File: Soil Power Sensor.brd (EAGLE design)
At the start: 94 x 67 mm, 92 parts, among them IC1 TPD2E2U06DCK, J1 12401832E402A, U1 MAX9943ATT+, U10 FT234XD, U11 ESP32-C3-MINI-1-N4, U2 INA296A5, U3 THS4532, U4 FSA2466, U5 MAX11201A, U6 REF2033, U7 TLV1117LV33, U8 LM27761DSG, U9 WIO E5, X1 Voltage, X2 Current, X3 GND, X4 SDI, X5 SMA-142-0701-801/806

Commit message: Updated consistent naming for components
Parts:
- C12, C17: value 4.7u -> 4.7uF
- C15: value 0.1u -> 0.1uF
- C16, C18: value 100n -> 100nF
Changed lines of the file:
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@@
 </autorouter>
 <elements>
-<element name="C12" library="rcl" library_urn="urn:adsk.eagle:library:334" package="C0603" package3d_urn="urn:adsk.eagle:package:23616/2" value="4.7u" x="55.88" y="40.64" smashed="yes" rot="R270">
+<element name="C12" library="rcl" library_urn="urn:adsk.eagle:library:334" package="C0603" package3d_urn="urn:adsk.eagle:package:23616/2" value="4.7uF" x="55.88" y="40.64" smashed="yes" rot="R270">
 <attribute name="NAME" x="54.483" y="38.989" size="1.27" layer="25" rot="R90"/>
 <attribute name="POPULARITY" value="73" x="-55.88" y="-45.72" size="1.778" layer="27" rot="R270" display="off"/>
@@
 <attribute name="SPICEPREFIX" value="C" x="142.24" y="-69.85" size="1.778" layer="27" display="off"/>
 </element>
-<element name="C15" library="rcl" library_urn="urn:adsk.eagle:library:334" package="C0603" package3d_urn="urn:adsk.eagle:package:23616/2" value="0.1u" x="73.66" y="24.13" smashed="yes" rot="R270">
+<element name="C15" library="rcl" library_urn="urn:adsk.eagle:library:334" package="C0603" package3d_urn="urn:adsk.eagle:package:23616/2" value="0.1uF" x="73.66" y="24.13" smashed="yes" rot="R270">
 <attribute name="NAME" x="74.803" y="25.781" size="1.27" layer="25" rot="R270"/>
 <attribute name="POPULARITY" value="73" x="-38.1" y="-67.31" size="1.778" layer="27" rot="R270" display="off"/>
 <attribute name="SPICEPREFIX" value="C" x="-38.1" y="-67.31" size="1.778" layer="27" rot="R270" display="off"/>
 </element>
-<element name="C18" library="rcl" library_urn="urn:adsk.eagle:library:334" package="C0603" package3d_urn="urn:adsk.eagle:package:23616/2" value="100n" x="66.04" y="63.5" smashed="yes">
+<element name="C18" library="rcl" library_urn="urn:adsk.eagle:library:334" package="C0603" package3d_urn="urn:adsk.eagle:package:23616/2" value="100nF" x="66.04" y="63.5" smashed="yes">
 <attribute name="NAME" x="64.389" y="64.643" size="1.27" layer="25"/>
 <attribute name="POPULARITY" value="73" x="96.52" y="-48.26" size="1.778" layer="27" display="off"/>
 <attribute name="SPICEPREFIX" value="C" x="96.52" y="-48.26" size="1.778" layer="27" display="off"/>
 </element>
-<element name="C16" library="rcl" library_urn="urn:adsk.eagle:library:334" package="C0603" package3d_urn="urn:adsk.eagle:package:23616/2" value="100n" x="71.12" y="63.5" smashed="yes">
+<element name="C16" library="rcl" library_urn="urn:adsk.eagle:library:334" package="C0603" package3d_urn="urn:adsk.eagle:package:23616/2" value="100nF" x="71.12" y="63.5" smashed="yes">
 <attribute name="NAME" x="69.469" y="64.643" size="1.27" layer="25"/>
 <attribute name="POPULARITY" value="73" x="107.95" y="-48.26" size="1.778" layer="27" display="off"/>
 <attribute name="SPICEPREFIX" value="C" x="107.95" y="-48.26" size="1.778" layer="27" display="off"/>
 </element>
-<element name="C17" library="rcl" library_urn="urn:adsk.eagle:library:334" package="C0603" package3d_urn="urn:adsk.eagle:package:23616/2" value="4.7u" x="71.12" y="58.42" smashed="yes">
+<element name="C17" library="rcl" library_urn="urn:adsk.eagle:library:334" package="C0603" package3d_urn="urn:adsk.eagle:package:23616/2" value="4.7uF" x="71.12" y="58.42" smashed="yes">
 <attribute name="NAME" x="69.723" y="59.563" size="1.27" layer="25"/>
 <attribute name="POPULARITY" value="73" x="167.64" y="-53.34" size="1.778" layer="27" display="off"/>

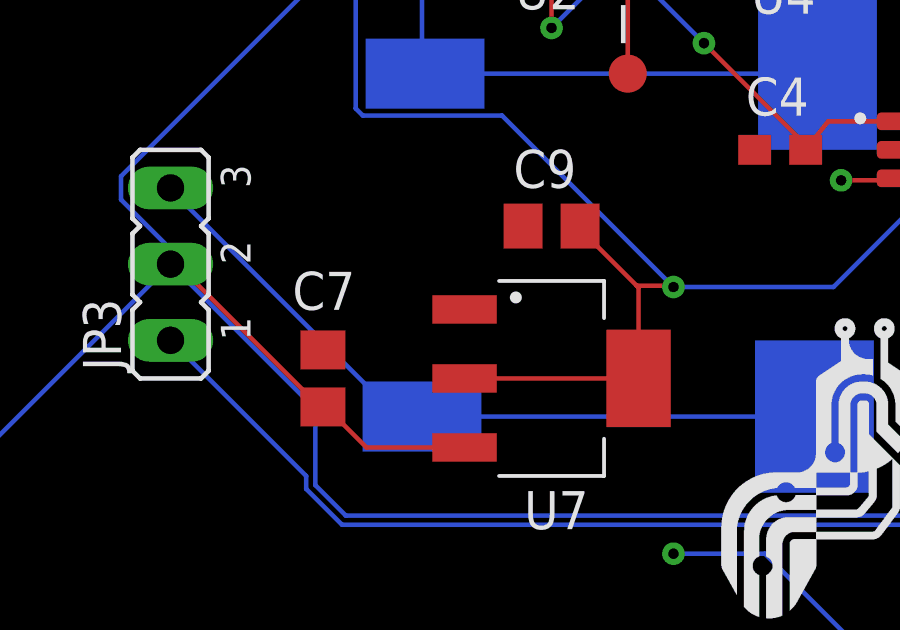
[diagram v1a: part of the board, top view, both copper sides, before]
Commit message: Added MPN to passive components
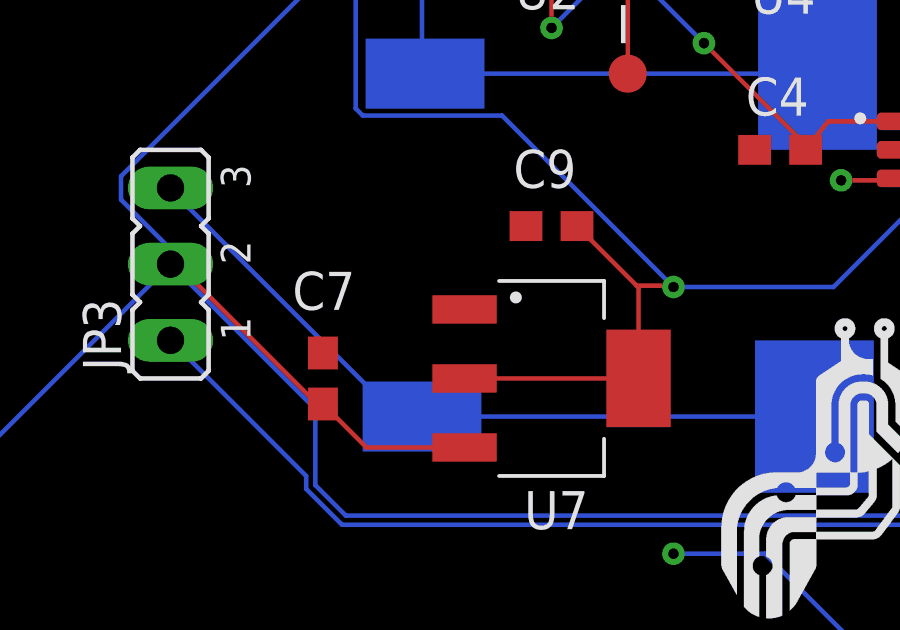
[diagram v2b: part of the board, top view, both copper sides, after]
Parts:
- C1: value 16uF -> 22pF
- C16, C18: value 100nF -> 0.1uF
- C2: value 20uF -> 27pF
- C7, C9: device rcl:C0805 -> rcl:C0603
- R6, R7: value 250k -> 249K

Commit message: Updated current sensing gains
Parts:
- R6, R7: value 249K -> 499K
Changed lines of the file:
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@@
 <drawing>
 <settings>
-<setting alwaysvectorfont="yes"/>
+<setting alwaysvectorfont="no"/>
 <setting verticaltext="up"/>
 </settings>
@@
 <attribute name="SPICEPREFIX" value="R" x="117.602" y="-48.768" size="1.778" layer="27" display="off"/>
 </element>
-<element name="R6" library="rcl" library_urn="urn:adsk.eagle:library:334" package="R0603" package3d_urn="urn:adsk.eagle:package:23555/3" value="249K" x="48.26" y="48.26" smashed="yes">
-<attribute name="MPN" value="RT0603BRD07249KL" x="48.26" y="48.26" size="1.778" layer="27" display="off"/>
+<element name="R6" library="rcl" library_urn="urn:adsk.eagle:library:334" package="R0603" package3d_urn="urn:adsk.eagle:package:23555/3" value="499K" x="48.26" y="48.26" smashed="yes">
+<attribute name="MPN" value="RT0603BRD07499KL" x="48.26" y="48.26" size="1.778" layer="27" display="off"/>
 <attribute name="NAME" x="47.117" y="48.895" size="1.27" layer="25"/>
 <attribute name="POPULARITY" value="77" x="124.46" y="-63.5" size="1.778" layer="27" display="off"/>
 <attribute name="SPICEPREFIX" value="R" x="124.46" y="-63.5" size="1.778" layer="27" display="off"/>
 </element>
-<element name="R7" library="rcl" library_urn="urn:adsk.eagle:library:334" package="R0603" package3d_urn="urn:adsk.eagle:package:23555/3" value="249K" x="48.26" y="50.8" smashed="yes">
-<attribute name="MPN" value="RT0603BRD07249KL" x="48.26" y="50.8" size="1.778" layer="27" display="off"/>
+<element name="R7" library="rcl" library_urn="urn:adsk.eagle:library:334" package="R0603" package3d_urn="urn:adsk.eagle:package:23555/3" value="499K" x="48.26" y="50.8" smashed="yes">
+<attribute name="MPN" value="RT0603BRD07499KL" x="48.26" y="50.8" size="1.778" layer="27" display="off"/>
 <attribute name="NAME" x="47.117" y="51.435" size="1.27" layer="25"/>
 <attribute name="POPULARITY" value="77" x="129.54" y="-60.96" size="1.778" layer="27" display="off"/>
